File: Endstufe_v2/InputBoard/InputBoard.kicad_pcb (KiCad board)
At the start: 4 copper layers, 85 x 50 mm, 65 parts, among them J1 ST-0322D00-071-1A2H, J11 DNP, J2 ST-0322D00-071-1A2H, J3 ST-0322D00-071-1A2H, J4 ST-0322D00-071-1A2H, J5 B4B-XH-2_(LF)(SN), J6 B4B-XH-2_(LF)(SN), J7 B4B-XH-2_(LF)(SN), J8 Conn_01x02_Pin, J9 B4B-XH-2_(LF)(SN), U1 PCM1865DBTR, U2 PCM9211PTR, U4 ZPLR135_T8, U5 ZPLR135_T8, U6 ZPLR135_T8, U7 ZPLR135_T8, Y1 24.576Mhz, Y2 24.576Mhz

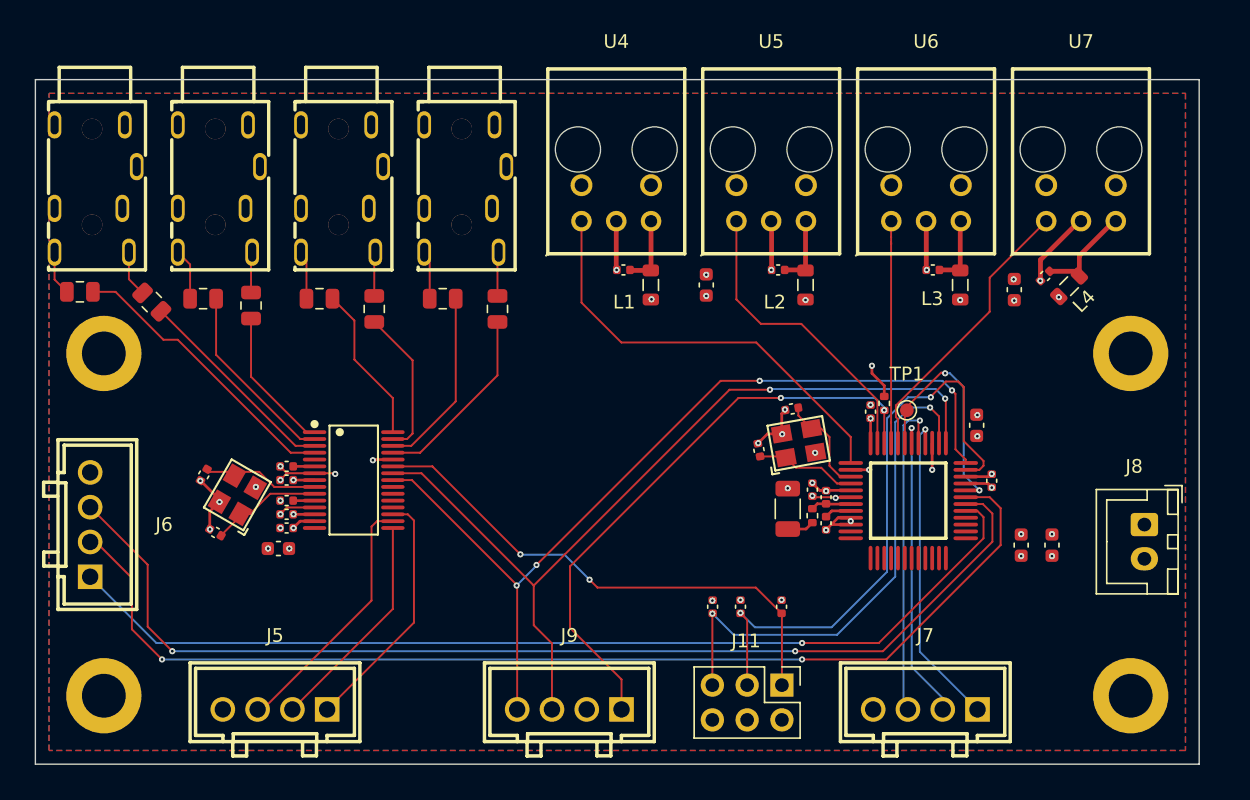
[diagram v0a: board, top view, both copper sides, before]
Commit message: Make boards compliant with JLCPCB
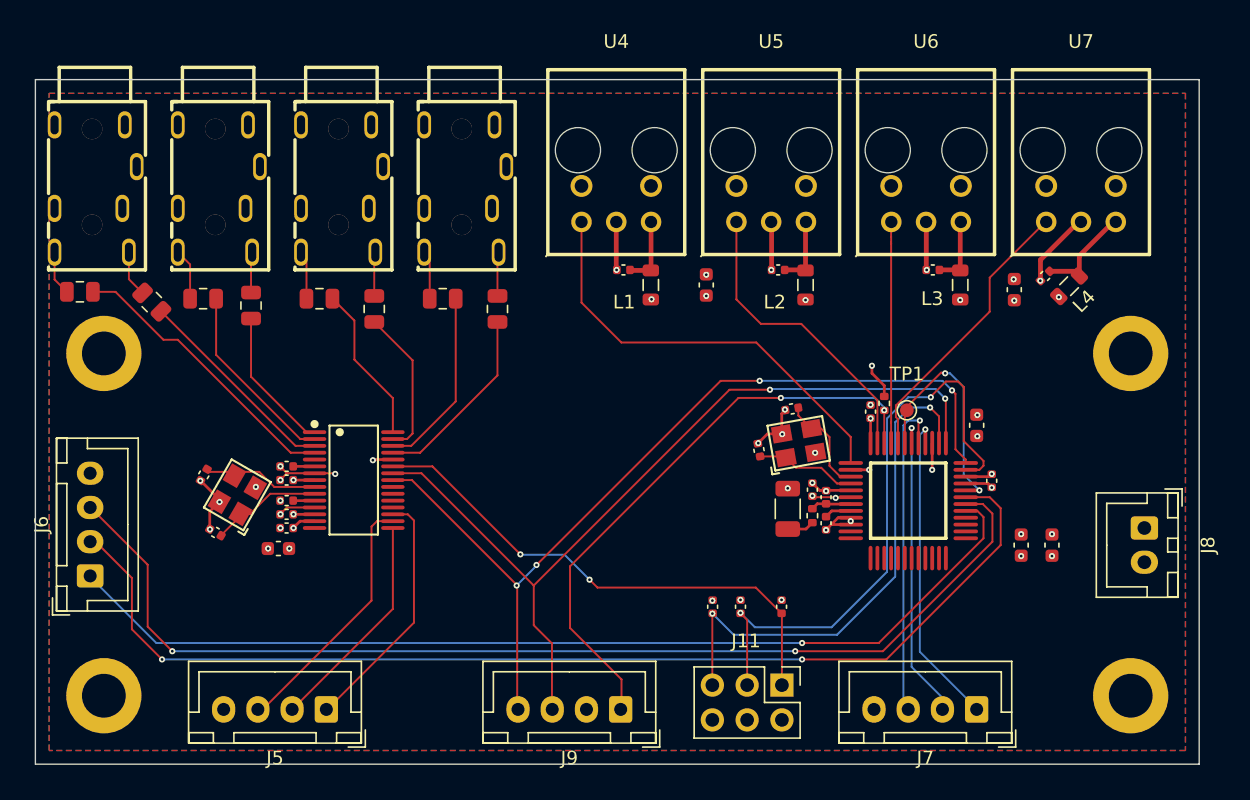
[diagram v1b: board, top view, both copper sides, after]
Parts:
- J5, J6, J7, J9: footprint Endstufe:CONN-TH_B4B-XH-2-LF-SN -> Endstufe:JST_XH_B4B-XH-A_1x04_P2.50mm_Vertical
- J8: footprint Connector_JST:JST_XH_B2B-XH-A_1x02_P2.50mm_Vertical -> Endstufe:JST_XH_B2B-XH-A_1x02_P2.50mm_Vertical
- moved J8 1.50 mm to (151.0, 104.0), turned to 90 degrees

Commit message: Change unavailable parts to available ones, optimise silkscreen, do via stiching
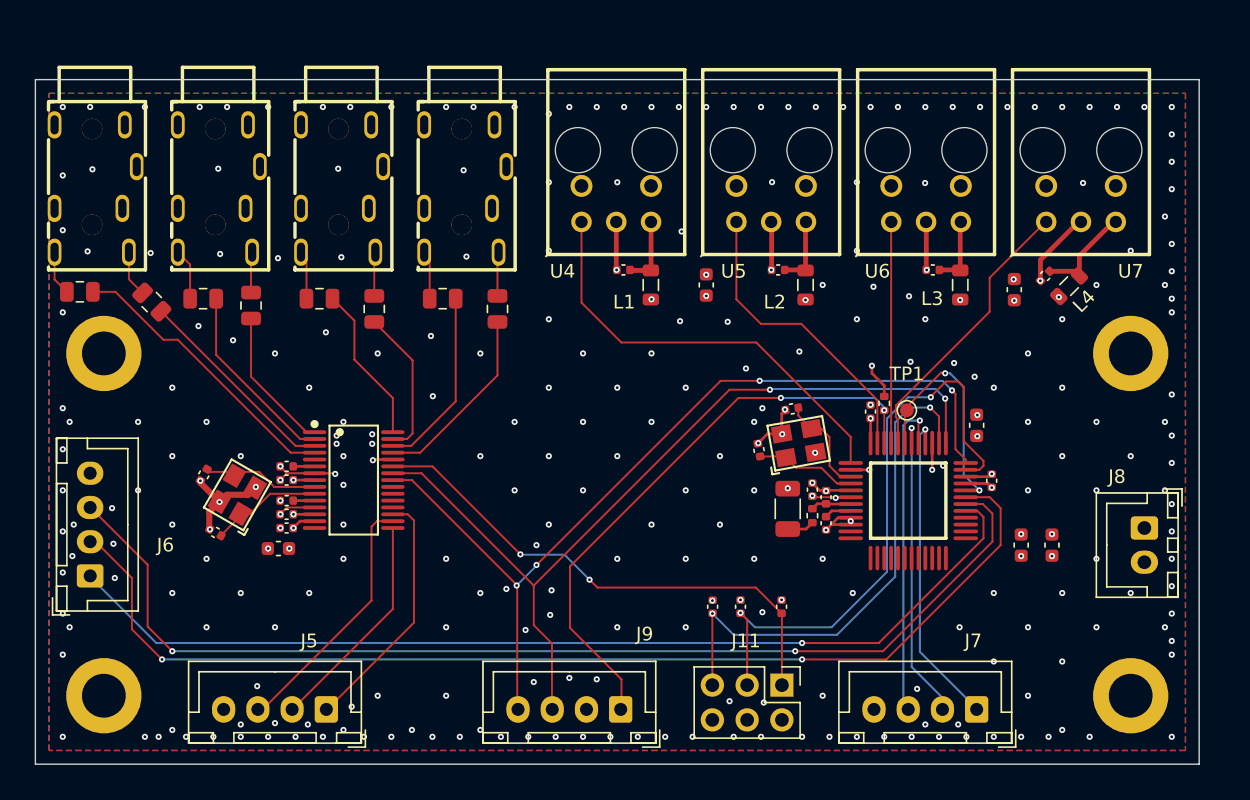
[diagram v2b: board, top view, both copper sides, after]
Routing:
- net GND: track 46.2 -> 49.4 mm, vias 37 -> 291
